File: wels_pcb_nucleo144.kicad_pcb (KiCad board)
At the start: 2 copper layers, 58 x 94.8 mm, 33 parts, among them J1 CN8, J10 SERVOMOTOR, J11 I2C PORT, J2 CN7, J3 CN10, J4 CN9, J5 SERVOMOTOR, J6 SD_CARD, J7 MLX90614, J8 MPU6050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

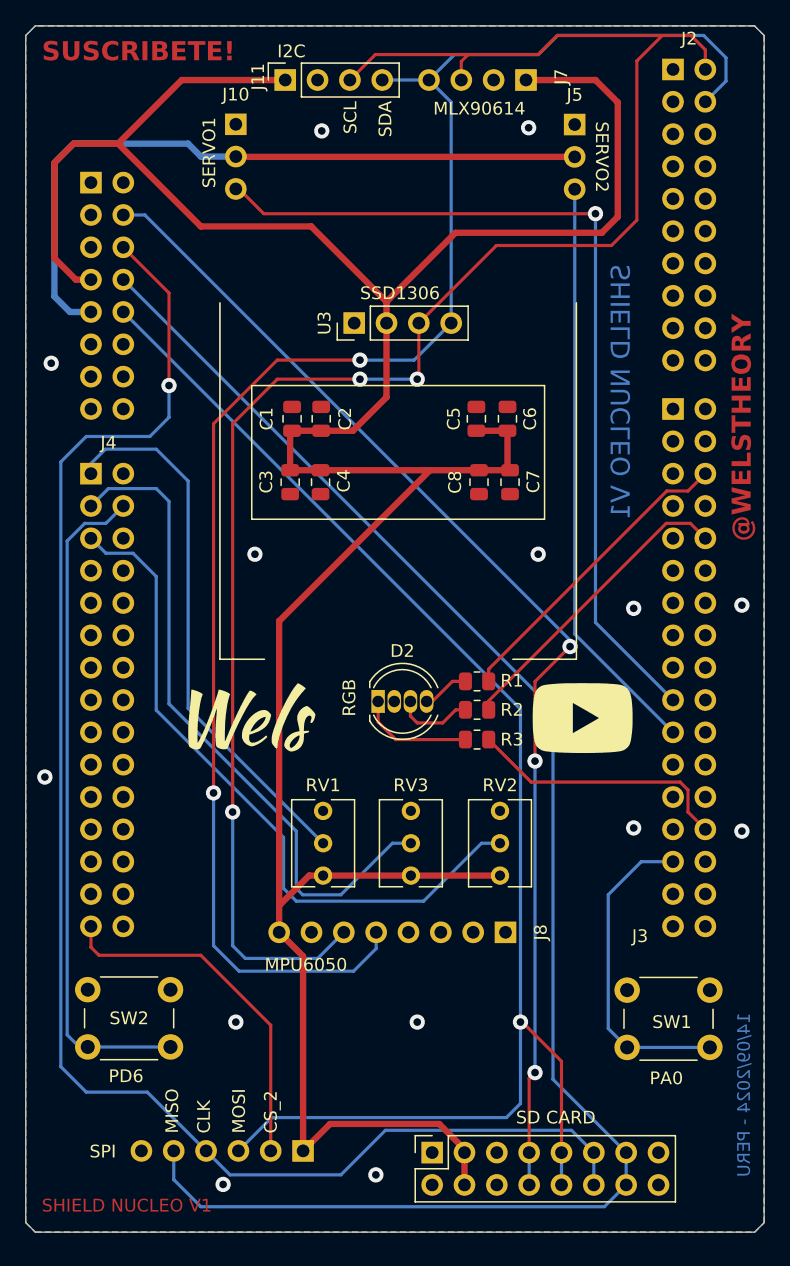
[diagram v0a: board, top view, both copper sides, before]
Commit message: Correccion alimentacion 5V para SD Card y cambio de footprint del LED RGB
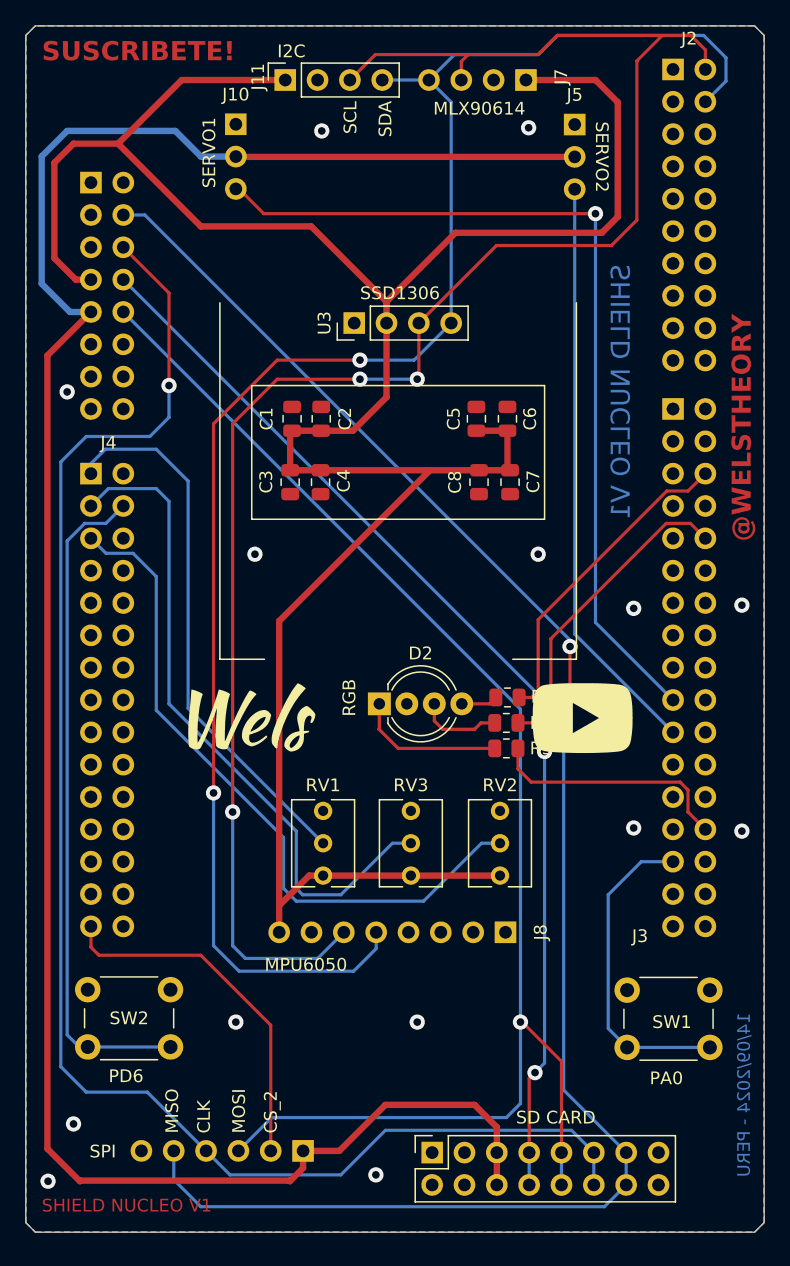
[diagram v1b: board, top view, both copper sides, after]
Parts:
- D2: footprint LED_THT:LED_D5.0mm-4_RGB -> LED_THT:LED_D5.0mm-4_RGB_Wide_Pins
- moved R1 2.70 mm to (144.6, 91.0)
- moved R2 2.52 mm to (144.5, 93.0)
- moved R3 2.40 mm to (144.5, 95.0)
- moved D2 0.21 mm to (134.5, 91.5)
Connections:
- J6 pad 3: +3V3 -> unconnected-(J6-Pin_3-Pad3)
- J6 pad 4: +3V3 -> unconnected-(J6-Pin_4-Pad4)
- J6 pad 5: unconnected-(J6-Pin_5-Pad5) -> +5V
- J6 pad 6: unconnected-(J6-Pin_6-Pad6) -> +5V
- J9 pad 1: +3V3 -> +5V
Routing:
- net +5V: track 55.8 -> 170.4 mm
- net +3V3: track 232.7 -> 197.6 mm
- net Net-(D2-BA): track 9.05 -> 11.7 mm
- net /PE14: track 21.0 -> 19.3 mm
- net /PE13: track 24.0 -> 25.0 mm
- net /PE11: track 24.3 -> 25.2 mm
